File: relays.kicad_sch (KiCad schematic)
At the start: 6 parts, among them K1 J107F1AS123VDC.36, K2 J107F1AS123VDC.36, K3 J107F1AS123VDC.36, Q1 2N2222A, Q2 2N2222A, Q3 2N2222A

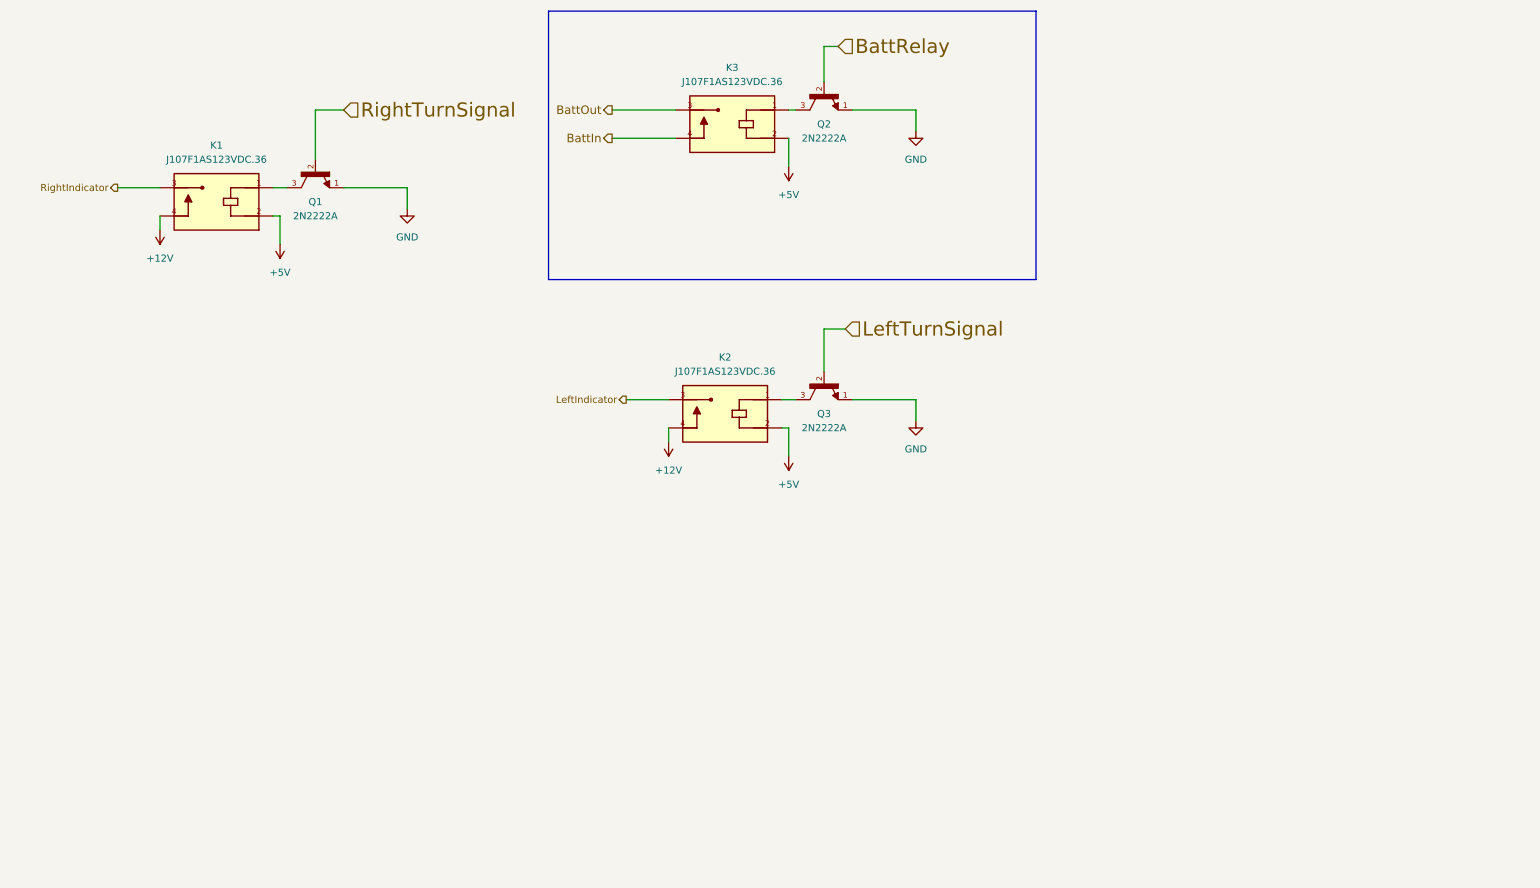
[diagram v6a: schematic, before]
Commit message: Final Pinout for connectors
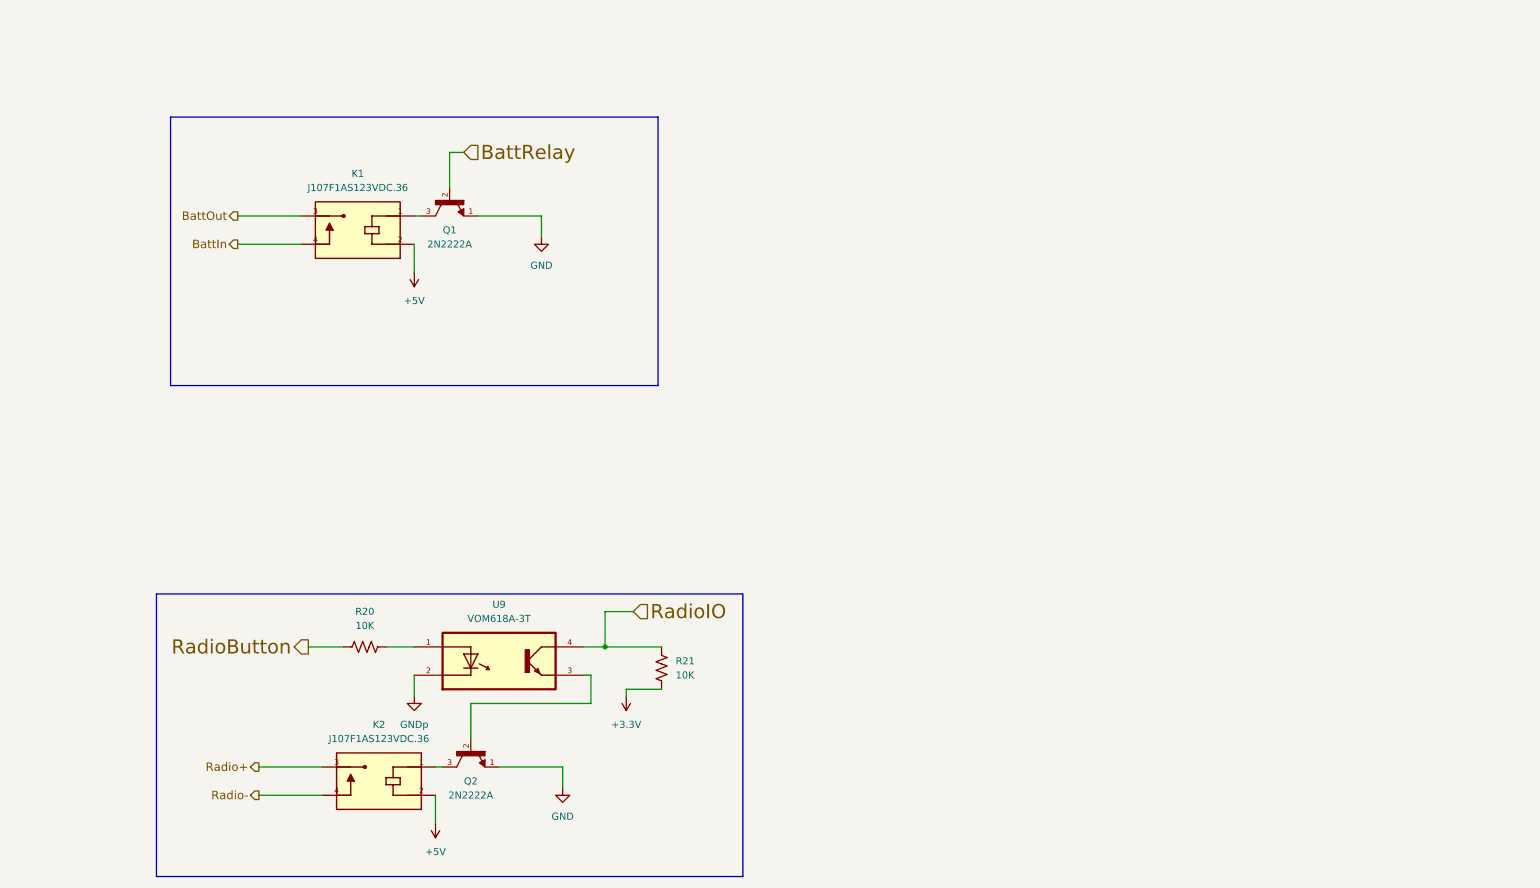
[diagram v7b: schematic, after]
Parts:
- removed K1: J107F1AS123VDC.36, PRE29-5V-S-450-1A-E:RELAY_PRE29-5V-S-450-1A-E, symbol PRE29-5V-S-450-1A-E:PRE29-5V-S-450-1A-E
- removed Q1, Q3: 2N2222A, 2N2222A:TO92254P470H750-3, symbol 2N2222A:2N2222A
- added Q2: 2N2222A, 2N2222A:TO92254P470H750-3, symbol 2N2222A:2N2222A
- added R20, R21: 10K, symbol Device:R_US
- added U9: VOM618A-3T, VOM618A-3T:SOIC254P695X242-4N, symbol VOM618A-3T:VOM618A-3T
- renumbered K3 to K1, Q2 to Q1
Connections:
- net GND: now also Q2.1
- net at K2.1: now also Q2.3
- net +12V renamed Radio-
- net LeftIndicator renamed Radio+
- new net: R20.2, U9.1
- new net: Q2.2, U9.3
- new net +3.3V: R21.2
- new net GNDp: U9.2
- new net RadioButton: R20.1
- new net RadioIO: R21.1, U9.4
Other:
- moved on the sheet: K1, Q1

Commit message: made connector match drawing
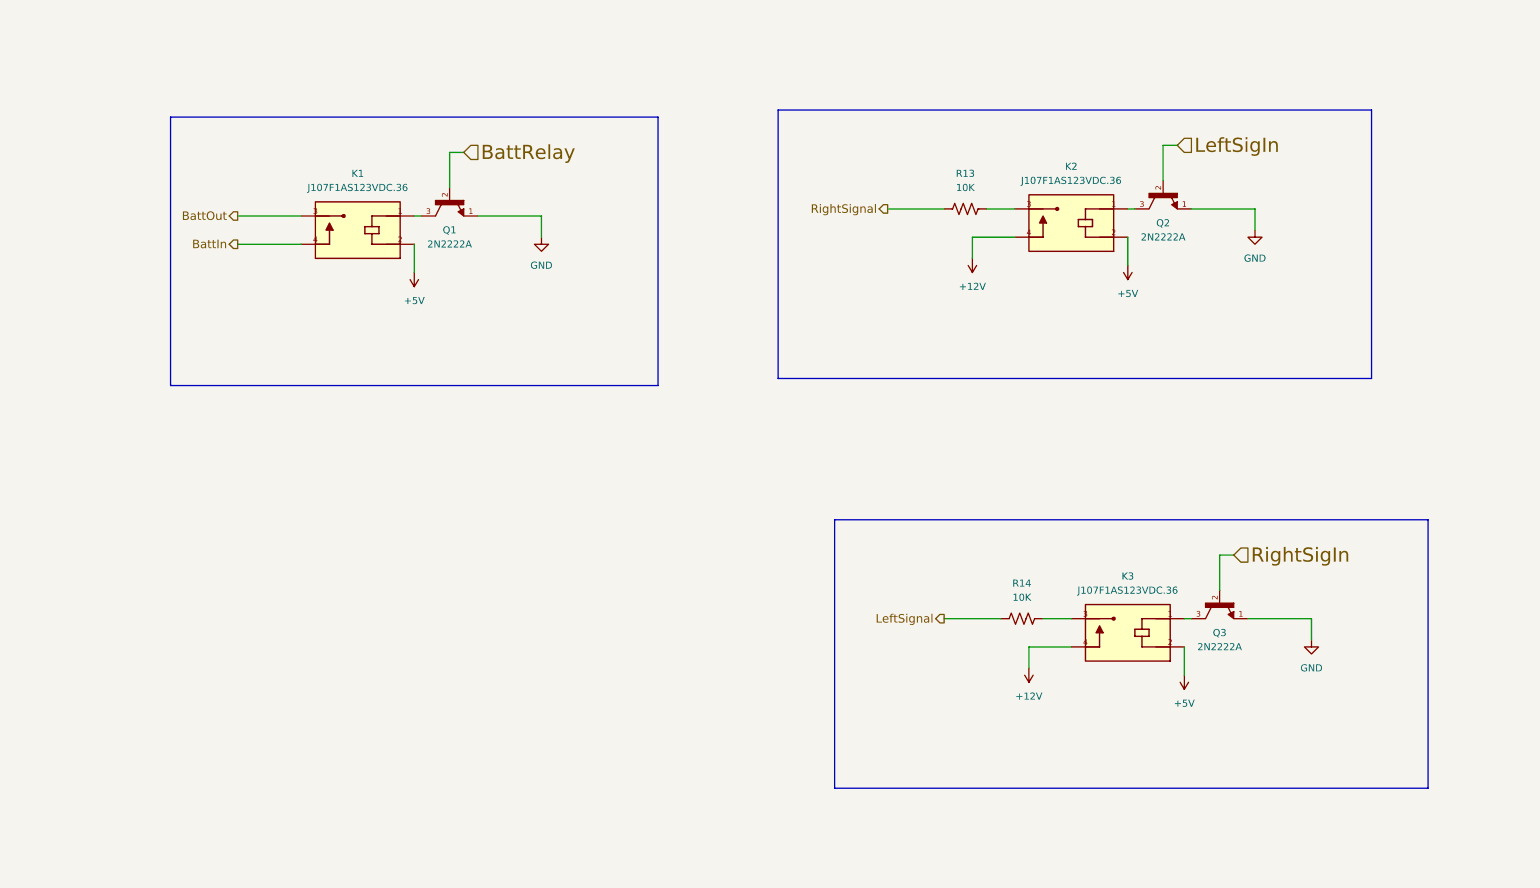
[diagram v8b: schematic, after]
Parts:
- removed R20, R21: 10K, symbol Device:R_US
- removed U9: VOM618A-3T, VOM618A-3T:SOIC254P695X242-4N, symbol VOM618A-3T:VOM618A-3T
- added K3: J107F1AS123VDC.36, PRE29-5V-S-450-1A-E:RELAY_PRE29-5V-S-450-1A-E, symbol PRE29-5V-S-450-1A-E:PRE29-5V-S-450-1A-E
- added Q3: 2N2222A, 2N2222A:TO92254P470H750-3, symbol 2N2222A:2N2222A
- added R13, R14: 10K, symbol Device:R_US
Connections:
- net +5V: now also K3.2
- net GND: now also Q3.1
- net LeftSigIn: now reaches Q2.2
- net Radio+: no longer names the net of K2.3
- net Radio+: now also R13.2
- net Radio- renamed +12V
- net +12V: now also K3.4
- new net: K3.1, Q3.3
- new net: K3.3, R14.2
- new net LeftSignal: R14.1
- new net RightSigIn: Q3.2
- new net RightSignal: R13.1
